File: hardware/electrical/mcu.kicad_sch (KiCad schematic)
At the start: 20 parts, among them SW1 B3U-1000P, U2 nRF52840, Y1 32 MHz Crystal

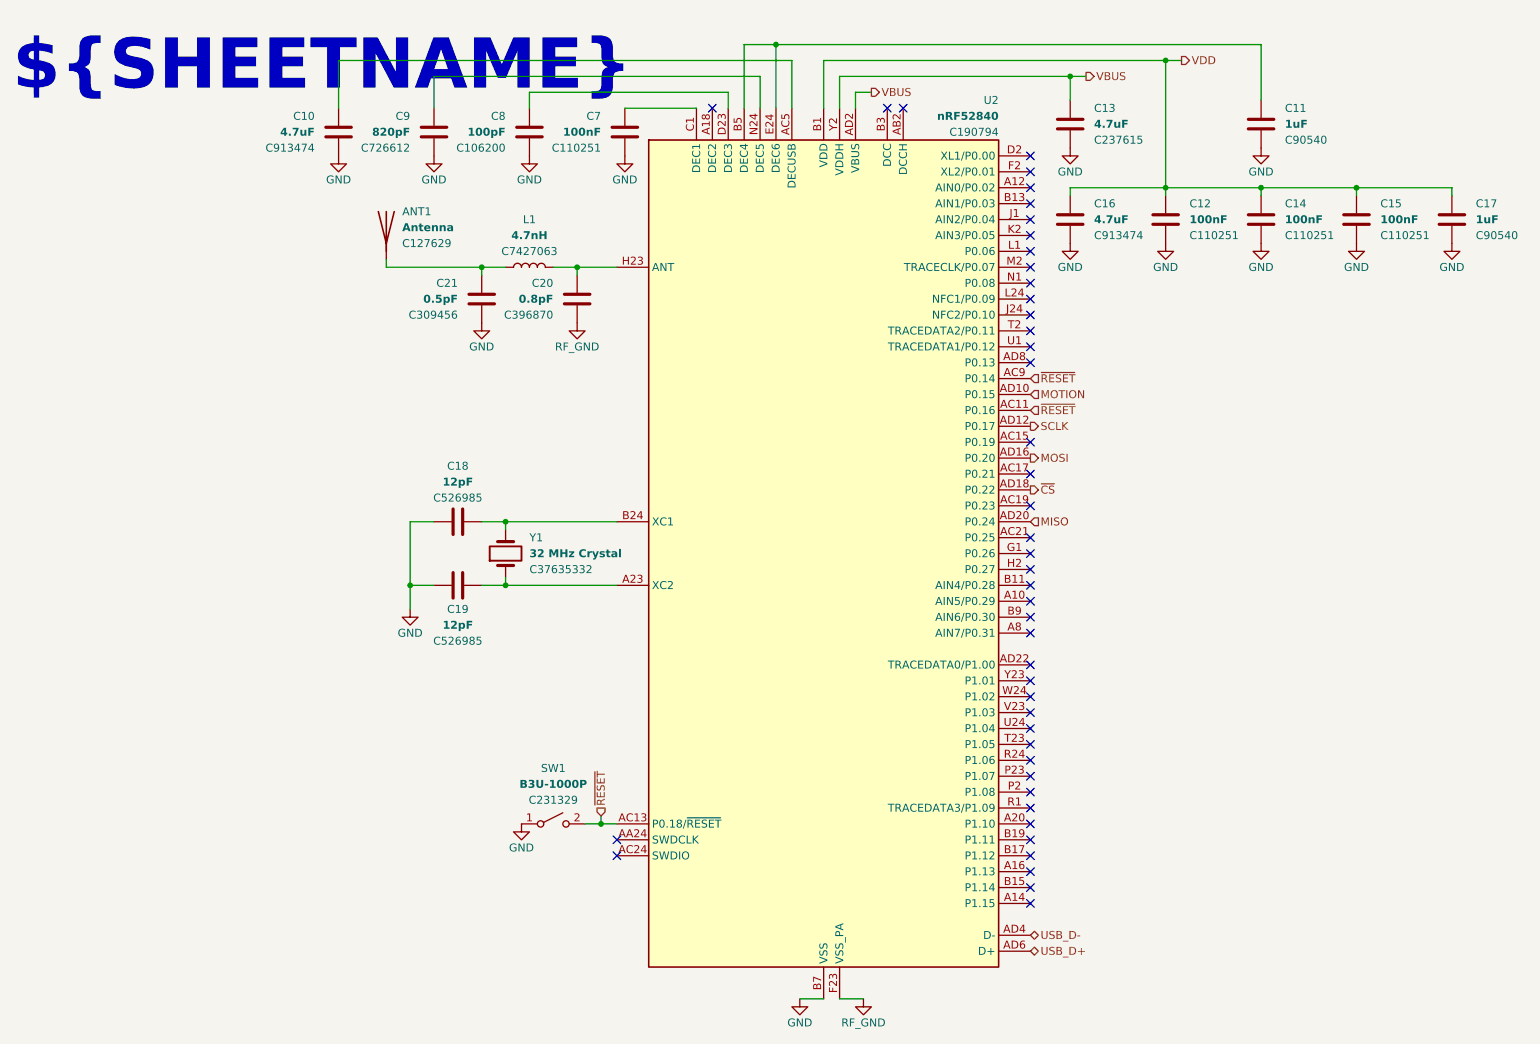
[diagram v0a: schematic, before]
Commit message: Update schematic to include regulators and switches, update render
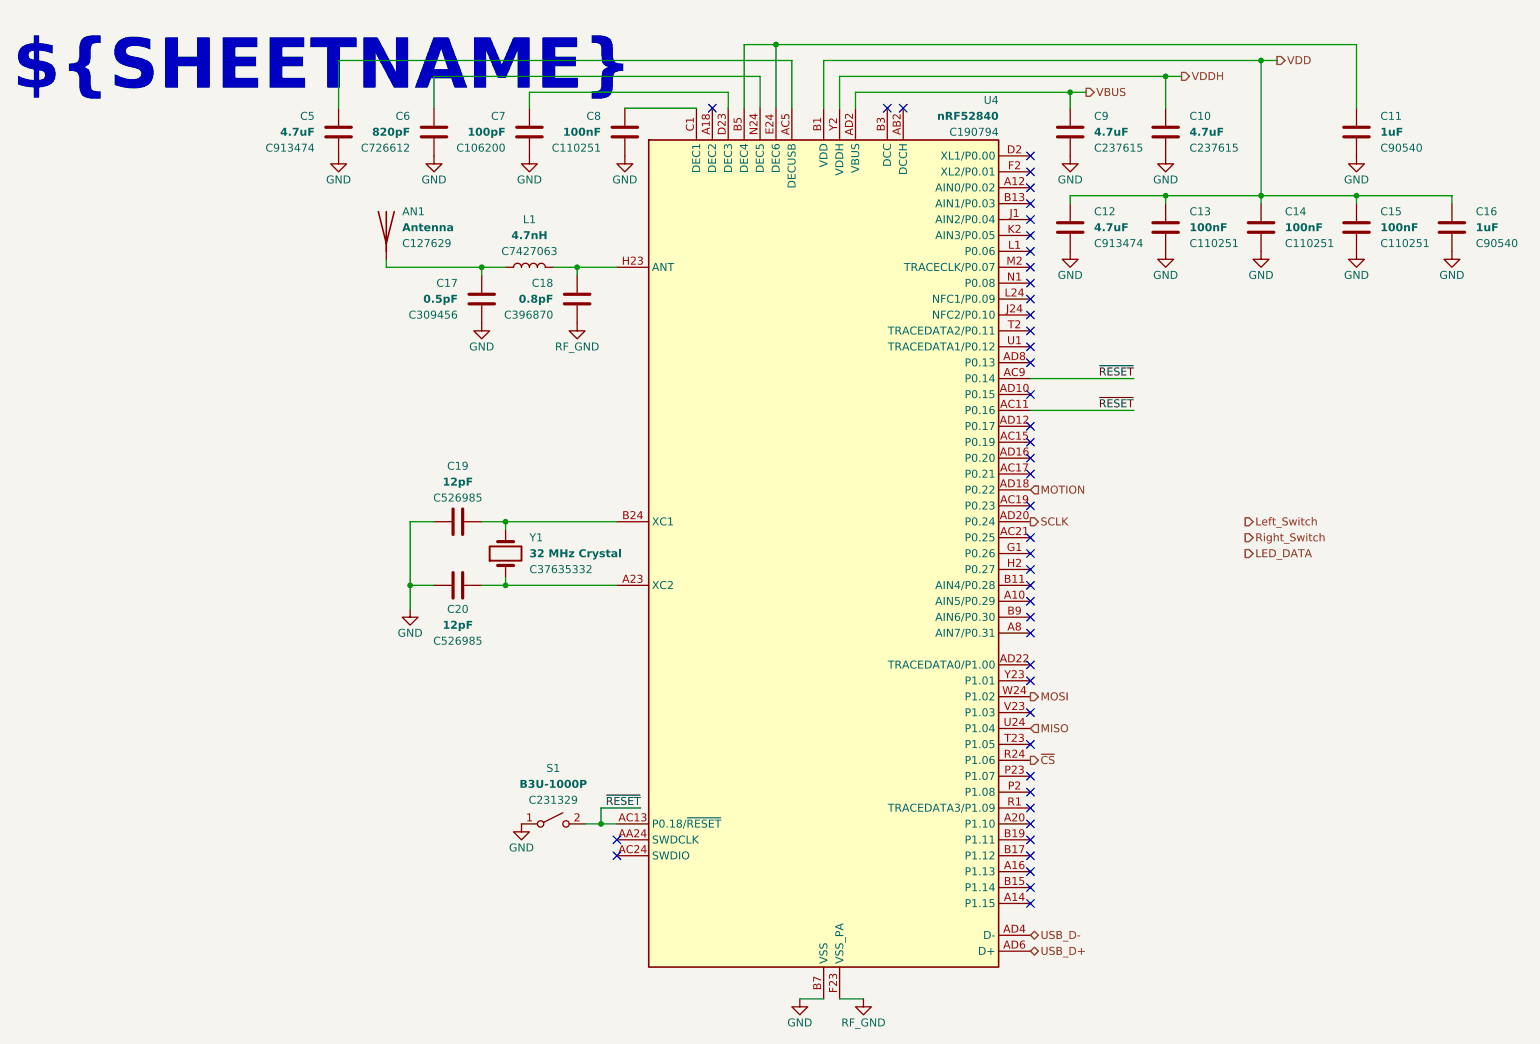
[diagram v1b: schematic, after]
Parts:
- added C9: 4.7uF, Capacitor_SMD:C_0603_1608Metric, symbol Device:C
- renumbered ANT1 to AN1, C13 to C10, C16 to C12, C12 to C13, C17 to C16, C21 to C17, C20 to C18, C18 to C19, C19 to C20, C10 to C5, C9 to C6, C8 to C7, C7 to C8, SW1 to S1, U2 to U4
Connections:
- net GND: now also C9.1
- net MISO: now also U4.U24 (P1.04); no longer U4.AD20 (P0.24)
- net MOSI: now also U4.W24 (P1.02); no longer U4.AD16 (P0.20)
- net MOTION: now also U4.AD18 (P0.22); no longer U4.AD10 (P0.15)
- net SCLK: now also U4.AD20 (P0.24); no longer U4.AD12 (P0.17)
- net VBUS: now also C9.2; no longer C10.2, U4.Y2 (VDDH)
- net ~{CS}: now also U4.R24 (P1.06); no longer U4.AD18 (P0.22)
- new net VDDH: C10.2, U4.Y2 (VDDH)
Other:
- moved on the sheet: C10, C11, C12, C13, C14, C15, C16
